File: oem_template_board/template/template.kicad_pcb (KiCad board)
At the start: 2 copper layers, 109.3 x 58.3 mm, 19 parts, among them U101 TPS560430YF

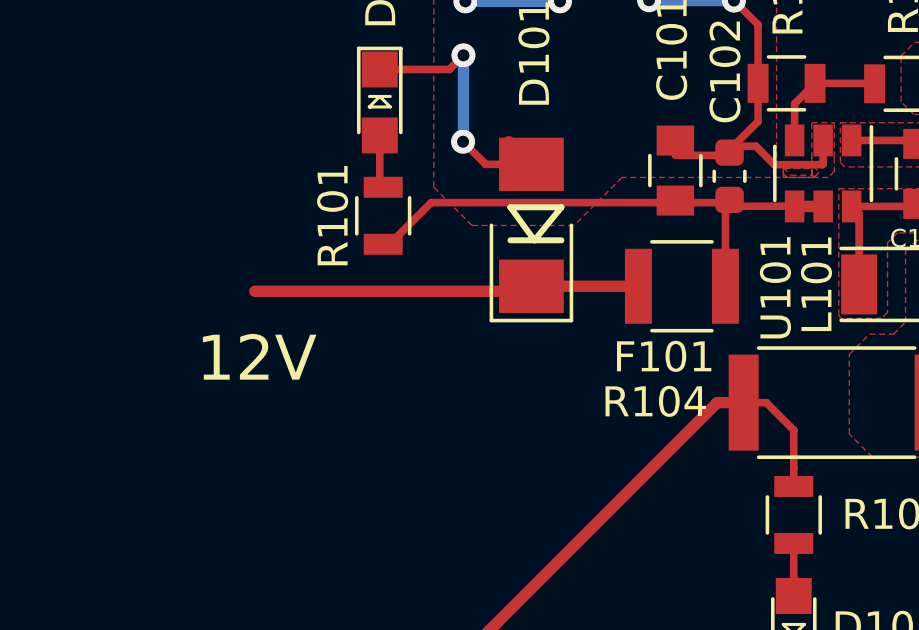
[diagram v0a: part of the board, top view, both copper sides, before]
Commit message: move fuse before zener diode so it pops during an over-voltage event
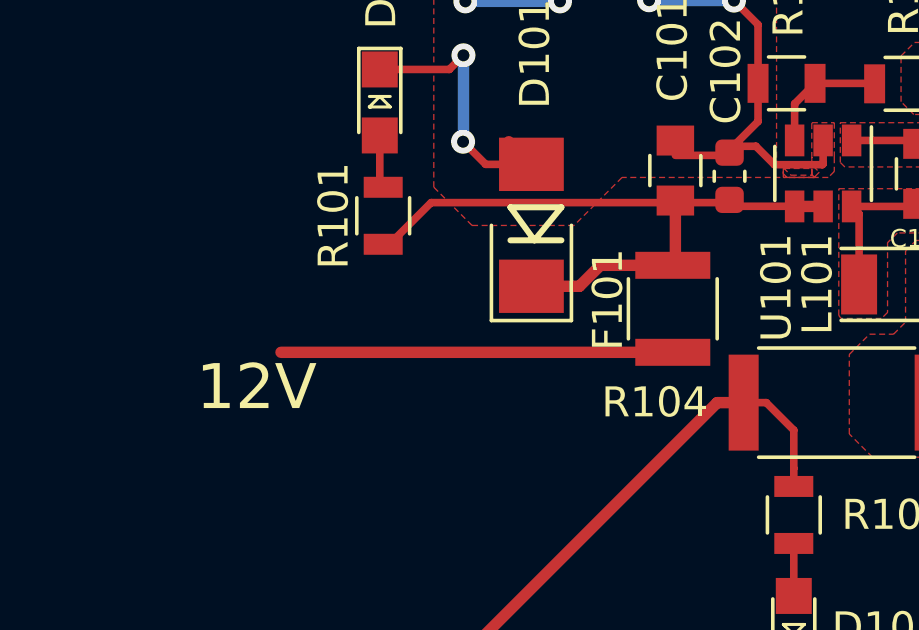
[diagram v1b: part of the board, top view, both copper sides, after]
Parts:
- moved F101 0.81 mm to (121.7, 106.5), turned to 270 degrees
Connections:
- COUT101 pad 2: Net-(COUT101-Pad2) -> GND
- COUT103 pad 2: Net-(COUT103-Pad2) -> GND
- D101 pad 1: /12V -> Net-(C101-Pad1)
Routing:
- net Net-(C101-Pad1): track 18.1 -> 22.9 mm
